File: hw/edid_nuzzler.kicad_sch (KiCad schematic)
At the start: 49 parts, among them J1 HDMI_A, J2 HDMI_A, J4 USB_C_Receptacle_USB2.0_16P, J5 Prog, Q1 BSS84AK, SW1 SW_Push, U1 74LVC1G3157, U2 74LVC1G3157, U3 CH340N, U4 CH32V003AxMx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

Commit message: Corase layout
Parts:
- TP1, TP10, TP11, TP12, TP13, TP14, TP4, TP6, TP7, TP8, TP9: value ~ -> pad; footprint nuzzler:Pin_tight -> TestPoint:TestPoint_Pad_D1.0mm
- TP2, TP3, TP5: footprint nuzzler:Pin_tight -> TestPoint:TestPoint_THTPad_D1.5mm_Drill0.7mm
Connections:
- net D2+: now reaches J1.1 (D2+), J2.1 (D2+)
- net CK+: now reaches J1.10 (CK+), J2.10 (CK+)
- net CK-: now reaches J1.12 (CK-), J2.12 (CK-)
- net D2-: now reaches J1.3 (D2-), J2.3 (D2-)
- net D1+: now reaches J1.4 (D1+), J2.4 (D1+)
- net D1-: now reaches J1.6 (D1-), J2.6 (D1-)
- net D0+: now reaches J1.7 (D0+), J2.7 (D0+)
- net D0-: now reaches J1.9 (D0-), J2.9 (D0-)
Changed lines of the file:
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@@
 		)
 	)
+	(label "D0-"
+		(at 52.07 40.64 0)
+		(effects
+			(font
+				(size 1.27 1.27)
+			)
+			(justify left bottom)
+		)
+	)
+	(label "CK+"
+		(at 52.07 43.18 0)
+		(effects
+			(font
+				(size 1.27 1.27)
+			)
+			(justify left bottom)
+		)
+	)
+	(label "CK-"
+		(at 52.07 45.72 0)
+		(effects
+			(font
+				(size 1.27 1.27)
+			)
+			(justify left bottom)
+		)
+	)
+	(label "D1-"
+		(at 52.07 35.56 0)
+		(effects
+			(font
+				(size 1.27 1.27)
+			)
+			(justify left bottom)
+		)
+	)
+	(label "D2-"
+		(at 52.07 30.48 0)
+		(effects
+			(font
+				(size 1.27 1.27)
+			)
+			(justify left bottom)
+		)
+	)
+	(label "D2+"
+		(at 52.07 27.94 0)
+		(effects
+			(font
+				(size 1.27 1.27)
+			)
+			(justify left bottom)
+		)
+	)
+	(label "D0+"
+		(at 52.07 38.1 0)
+		(effects
+			(font
+				(size 1.27 1.27)
+			)
+			(justify left bottom)
+		)
+	)
+	(label "D1+"
+		(at 52.07 33.02 0)
+		(effects
+			(font
+				(size 1.27 1.27)
+			)
+			(justify left bottom)
+		)
+	)
 	(symbol
 		(lib_id "power:GND")
@@
 			)
 		)
-		(property "Value" "~"
+		(property "Value" "pad"
 			(at 99.06 133.35 0)
 			(effects
@@
 			)
 		)
-		(property "Footprint" "nuzzler:Pin_tight"
+		(property "Footprint" "TestPoint:TestPoint_Pad_D1.0mm"
 			(at 102.87 132.08 0)
 			(effects
@@
 			)
 		)
-		(property "Value" "~"
+		(property "Value" "pad"
 			(at 99.06 130.81 0)
 			(effects
@@
 			)
 		)
-		(property "Footprint" "nuzzler:Pin_tight"
+		(property "Footprint" "TestPoint:TestPoint_Pad_D1.0mm"
 			(at 102.87 129.54 0)
 			(effects
@@
 			)
 		)
-		(property "Value" "~"
+		(property "Value" "pad"
 			(at 99.06 128.27 0)
 			(effects
@@
 			)
 		)
-		(property "Footprint" "nuzzler:Pin_tight"
+		(property "Footprint" "TestPoint:TestPoint_Pad_D1.0mm"
 			(at 102.87 127 0)
 			(effects
@@
 			)
 		)
-		(property "Value" "~"
+		(property "Value" "pad"
 			(at 76.2 138.43 0)
 			(effects
@@
 			)
 		)
-		(property "Footprint" "nuzzler:Pin_tight"
+		(property "Footprint" "TestPoint:TestPoint_Pad_D1.0mm"
 			(at 72.39 137.16 0)
 			(effects
@@
 			)
 		)
-		(property "Value" "~"
+		(property "Value" "pad"
 			(at 76.2 140.97 0)
 			(effects
@@
 			)
 		)
-		(property "Footprint" "nuzzler:Pin_tight"
+		(property "Footprint" "TestPoint:TestPoint_Pad_D1.0mm"
 			(at 72.39 139.7 0)
 			(effects
@@
 			)
 		)
-		(property "Value" "~"
+		(property "Value" "pad"
 			(at 76.2 133.35 0)
 			(effects
@@
 			)
 		)
-		(property "Footprint" "nuzzler:Pin_tight"
+		(property "Footprint" "TestPoint:TestPoint_Pad_D1.0mm"
 			(at 72.39 132.08 0)
 			(effects
@@
 			)
 		)
-		(property "Footprint" "nuzzler:Pin_tight"
+		(property "Footprint" "TestPoint:TestPoint_THTPad_D1.5mm_Drill0.7mm"
 			(at 72.39 127 0)
 			(effects
@@
 			)
 		)
-		(property "Value" "~"
+		(property "Value" "pad"
 			(at 99.06 146.05 0)
 			(effects
@@
 			)
 		)
-		(property "Footprint" "nuzzler:Pin_tight"
+		(property "Footprint" "TestPoint:TestPoint_Pad_D1.0mm"
 			(at 102.87 144.78 0)
 			(effects
@@
 			)
 		)
-		(property "Value" "~"
+		(property "Value" "pad"
 			(at 76.2 125.73 0)
 			(effects
@@
 			)
 		)
-		(property "Footprint" "nuzzler:Pin_tight"
+		(property "Footprint" "TestPoint:TestPoint_Pad_D1.0mm"
 			(at 72.39 124.46 0)
 			(effects
@@
 			)
 		)
-		(property "Value" "~"
+		(property "Value" "pad"
 			(at 99.06 143.51 0)
 			(effects
@@
 			)
 		)
-		(property "Footprint" "nuzzler:Pin_tight"
+		(property "Footprint" "TestPoint:TestPoint_Pad_D1.0mm"
 			(at 102.87 142.24 0)
 			(effects
@@
 			)
 		)
-		(property "Footprint" "nuzzler:Pin_tight"
+		(property "Footprint" "TestPoint:TestPoint_THTPad_D1.5mm_Drill0.7mm"
 			(at 72.39 129.54 0)
 			(effects
@@
 			)
 		)
-		(property "Value" "~"
+		(property "Value" "pad"
 			(at 99.06 125.73 0)
 			(effects
@@
 			)
 		)
-		(property "Footprint" "nuzzler:Pin_tight"
+		(property "Footprint" "TestPoint:TestPoint_Pad_D1.0mm"
 			(at 92.71 124.46 0)
 			(effects
@@
 			)
 		)
-		(property "Footprint" "nuzzler:Pin_tight"
+		(property "Footprint" "TestPoint:TestPoint_THTPad_D1.5mm_Drill0.7mm"
 			(at 72.39 134.62 0)
 			(effects
@@
 			)
 		)
-		(property "Value" "~"
+		(property "Value" "pad"
 			(at 99.06 135.89 0)
 			(effects
@@
 			)
 		)
-		(property "Footprint" "nuzzler:Pin_tight"
+		(property "Footprint" "TestPoint:TestPoint_Pad_D1.0mm"
 			(at 102.87 134.62 0)
 			(effects

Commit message: Rough idea about routing
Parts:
- removed C6: 1u, Capacitor_SMD:C_0603_1608Metric_Pad1.08x0.95mm_HandSolder, symbol Device:C_Small
- removed J5: Prog, nuzzler:PinHeader_1x03_P2.54mm_Vertical_Tight, symbol Connector_Generic:Conn_01x03
- removed R11: 5k1, Resistor_SMD:R_0603_1608Metric_Pad0.98x0.95mm_HandSolder, symbol Device:R_Small
- removed TP2, TP3, TP5: ~, TestPoint:TestPoint_THTPad_D1.5mm_Drill0.7mm, symbol Connector:TestPoint_Small
- removed TP8: pad, TestPoint:TestPoint_Pad_D1.0mm, symbol Connector:TestPoint_Small
- removed U6: ZD24C16A-STGMT, Package_TO_SOT_SMD:SOT-23-5, symbol Memory_EEPROM:AT24CS16-STUM
- added J3: Conn_02x03_Counter_Clockwise, Connector_PinHeader_2.54mm:PinHeader_2x03_P2.54mm_Vertical, symbol Connector_Generic:Conn_02x03_Counter_Clockwise
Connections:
- net GND: now also J3.1 (Pin_1)
- net at R1.2, U2.3, U4.7 (PD1): now also J3.3 (Pin_3)
- net at C1.1, C2.1, C3.1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: now also J3.2 (Pin_2)
- net at J1.15 (SCL), R6.2, U2.1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: now also J3.6 (Pin_6)
- net at J1.16 (SDA), R7.2, U1.1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: now also J3.4 (Pin_4)
- net UD+: now reaches J4.A6 (D+), J4.B6 (D+), U3.1 (UD+)
- net UD-: now reaches J4.A7 (D-), J4.B7 (D-), U3.2 (UD-)
- net at J1.19 (HPD), R10.1, U5.4: now also J3.5 (Pin_5)

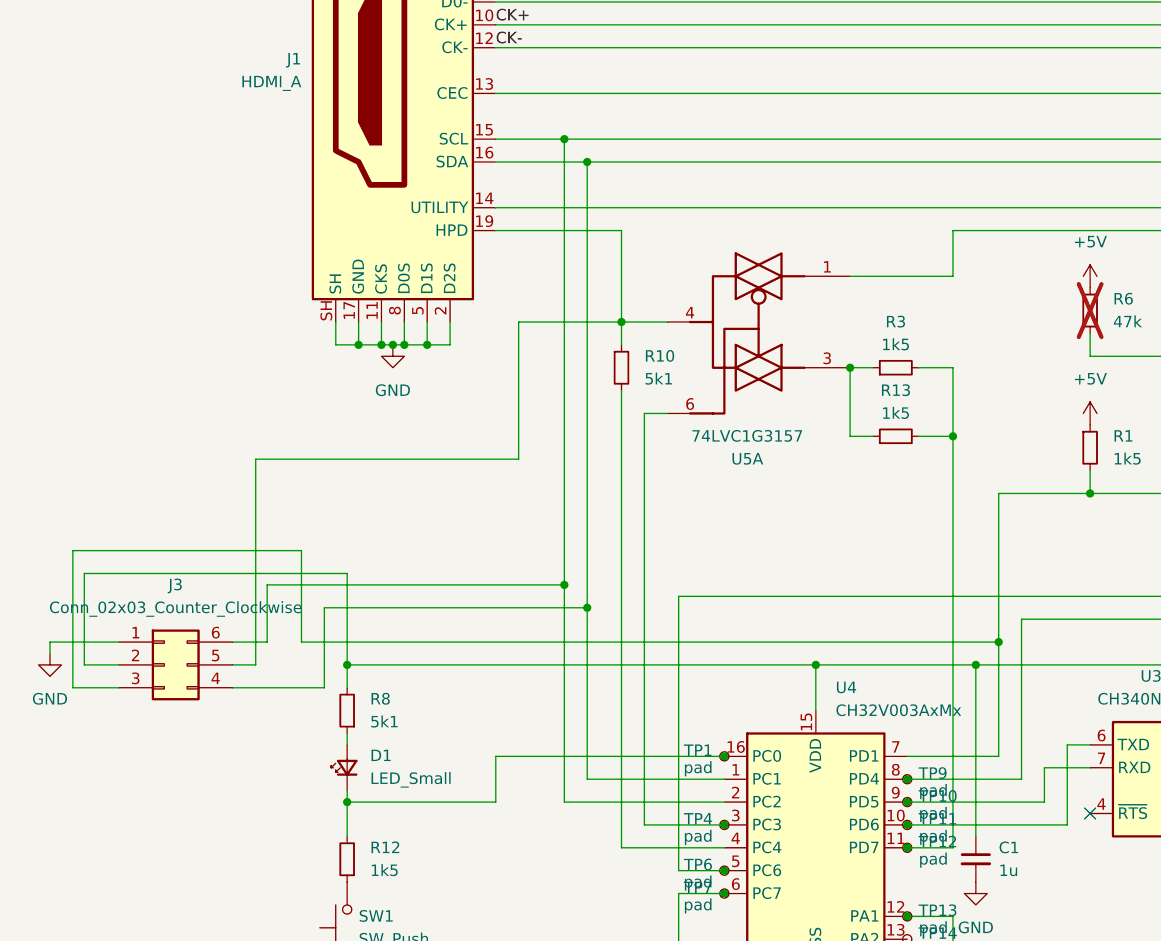
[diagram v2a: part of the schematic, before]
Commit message: Sync J3 sch symbol numbering order with the pcb footprint
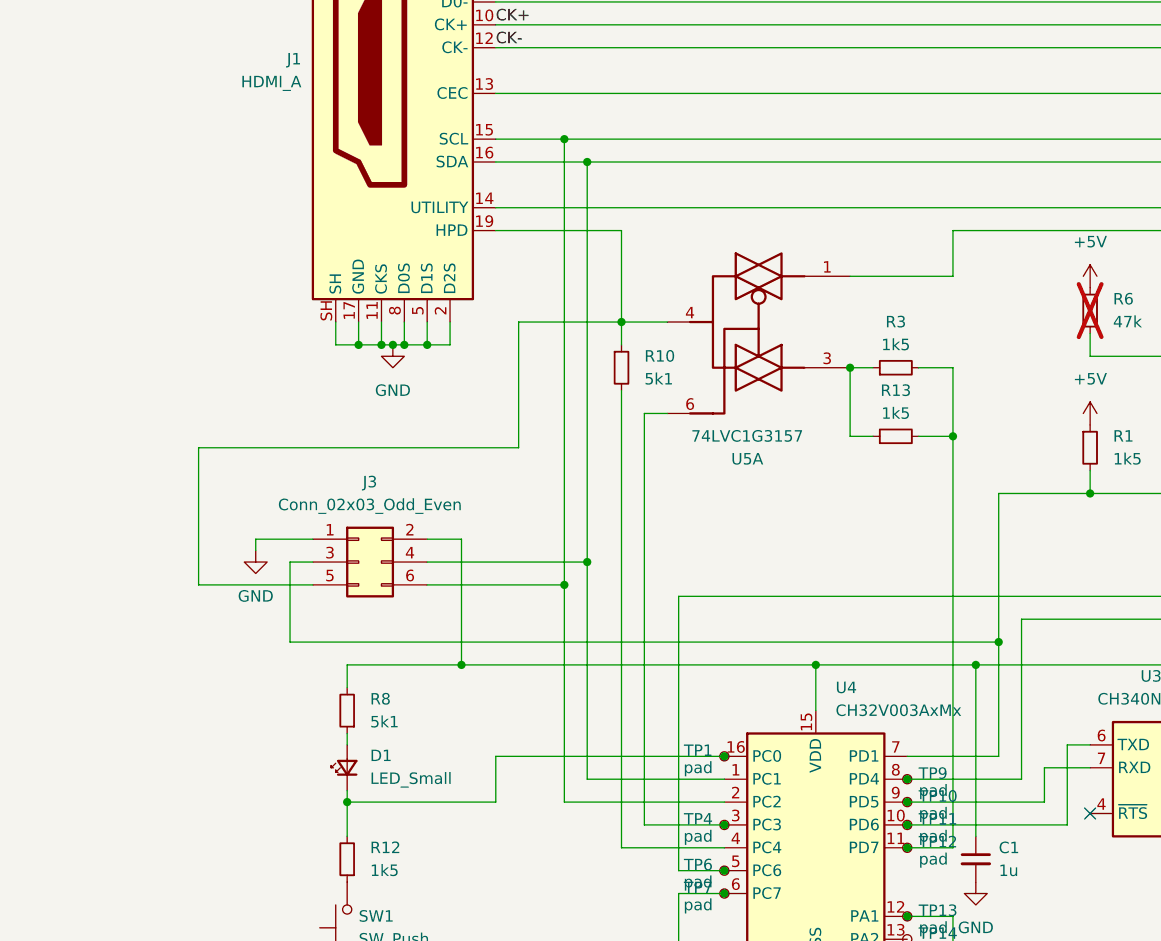
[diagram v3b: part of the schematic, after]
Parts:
- removed J3: Conn_02x03_Counter_Clockwise, Connector_PinHeader_2.54mm:PinHeader_2x03_P2.54mm_Vertical, symbol Connector_Generic:Conn_02x03_Counter_Clockwise
- added J3: Conn_02x03_Odd_Even, symbol Connector_Generic:Conn_02x03_Odd_Even
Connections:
- net GND: now also J3.1 (Pin_1)
- net at R1.2, U2.3, U4.7 (PD1): now also J3.3 (Pin_3)
- net at C1.1, C2.1, C3.1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: now also J3.2 (Pin_2)
- net at J1.15 (SCL), R6.2, U2.1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: now also J3.6 (Pin_6)
- net at J1.16 (SDA), R7.2, U1.1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: now also J3.4 (Pin_4)
- net at J1.19 (HPD), R10.1, U5.4: now also J3.5 (Pin_5)
